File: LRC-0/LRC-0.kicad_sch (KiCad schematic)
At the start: 69 parts, among them J1 USB_C_Receptacle_USB2.0_14P, J2 Battery, J3 Conn_01x10, J4 SMA, J5 u.FL, SW1 EN, SW2 BOOT, U1 AP7361C-33E, U2 TVS1400DRV, U3 BQ24075RGT, U4 ESP32-C6-MINI-1, U5 SX1262IMLTRT, U6 4259-63, U8 4259-63, Y1 TX32-33015S-32.000-X-R

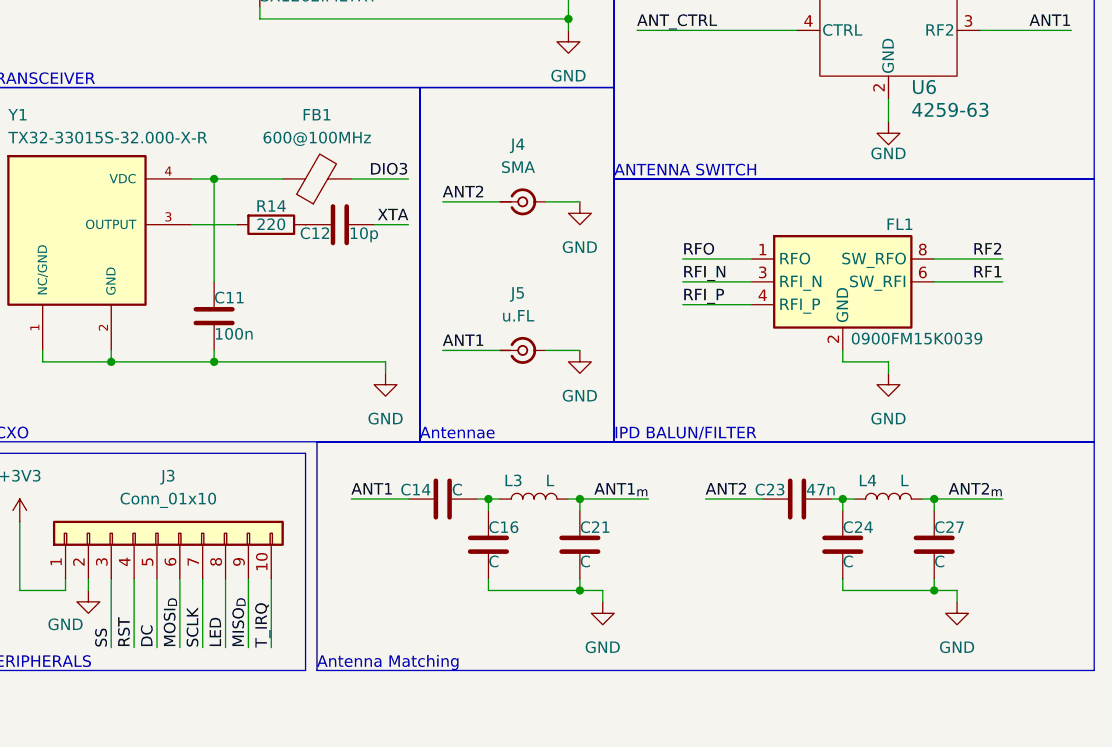
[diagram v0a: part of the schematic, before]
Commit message: rf route for filter and transceiver
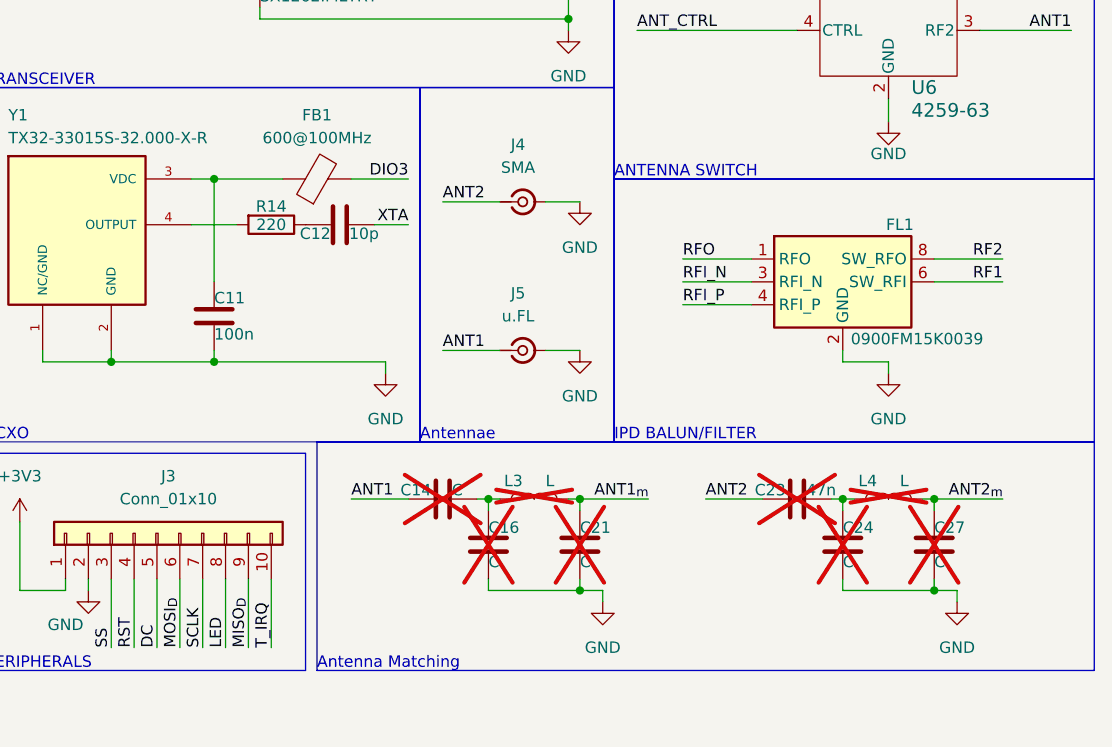
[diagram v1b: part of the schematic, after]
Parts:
- C14, C16, C21, C23, C24, C27, L3, L4: now not fitted
- L2: footprint Inductor_SMD:L_0402_1005Metric -> Inductor_SMD:L_0603_1608Metric
- U4: footprint RF_Module:ESP32-C6-MINI-1 -> ESP32_C6_MINI_1U_H4:XCVR_ESP32-C6-MINI-1U-H4
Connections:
- net at C11.1, FB1.1: now also Y1.3 (VDC); no longer Y1.4 (VDC)
- net at R14.2: now also Y1.4 (OUTPUT); no longer Y1.3 (OUTPUT)

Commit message: first pass done
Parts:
- C14, C16, C21, C23, C24, C27, L3, L4: now left out of the parts list
- L2: footprint Inductor_SMD:L_0603_1608Metric -> Inductor_SMD:L_1008_2520Metric
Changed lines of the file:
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@@
 		(unit 1)
 		(body_style 1)
-		(exclude_from_sim no)
-		(in_bom yes)
-		(on_board yes)
-		(in_pos_files yes)
+		(exclude_from_sim yes)
+		(in_bom no)
+		(on_board no)
+		(in_pos_files no)
 		(dnp yes)
 		(property "Reference" "C14"
@@
 		(unit 1)
 		(body_style 1)
-		(exclude_from_sim no)
-		(in_bom yes)
-		(on_board yes)
-		(in_pos_files yes)
+		(exclude_from_sim yes)
+		(in_bom no)
+		(on_board no)
+		(in_pos_files no)
 		(dnp yes)
 		(property "Reference" "C21"
@@
 		(unit 1)
 		(body_style 1)
-		(exclude_from_sim no)
-		(in_bom yes)
-		(on_board yes)
-		(in_pos_files yes)
+		(exclude_from_sim yes)
+		(in_bom no)
+		(on_board no)
+		(in_pos_files no)
 		(dnp yes)
 		(property "Reference" "L3"
@@
 		(unit 1)
 		(body_style 1)
-		(exclude_from_sim no)
-		(in_bom yes)
-		(on_board yes)
-		(in_pos_files yes)
+		(exclude_from_sim yes)
+		(in_bom no)
+		(on_board no)
+		(in_pos_files no)
 		(dnp yes)
 		(property "Reference" "C23"
@@
 		(unit 1)
 		(body_style 1)
-		(exclude_from_sim no)
-		(in_bom yes)
-		(on_board yes)
-		(in_pos_files yes)
+		(exclude_from_sim yes)
+		(in_bom no)
+		(on_board no)
+		(in_pos_files no)
 		(dnp yes)
 		(property "Reference" "C16"
@@
 		(unit 1)
 		(body_style 1)
-		(exclude_from_sim no)
-		(in_bom yes)
-		(on_board yes)
-		(in_pos_files yes)
+		(exclude_from_sim yes)
+		(in_bom no)
+		(on_board no)
+		(in_pos_files no)
 		(dnp yes)
 		(property "Reference" "C27"
@@
 			)
 		)
-		(property "Footprint" "Inductor_SMD:L_0603_1608Metric"
+		(property "Footprint" "Inductor_SMD:L_1008_2520Metric"
 			(at 195.58 40.64 0)
 			(hide yes)
@@
 		(unit 1)
 		(body_style 1)
-		(exclude_from_sim no)
-		(in_bom yes)
-		(on_board yes)
-		(in_pos_files yes)
+		(exclude_from_sim yes)
+		(in_bom no)
+		(on_board no)
+		(in_pos_files no)
 		(dnp yes)
 		(property "Reference" "C24"
@@
 		(unit 1)
 		(body_style 1)
-		(exclude_from_sim no)
-		(in_bom yes)
-		(on_board yes)
-		(in_pos_files yes)
+		(exclude_from_sim yes)
+		(in_bom no)
+		(on_board no)
+		(in_pos_files no)
 		(dnp yes)
 		(property "Reference" "L4"

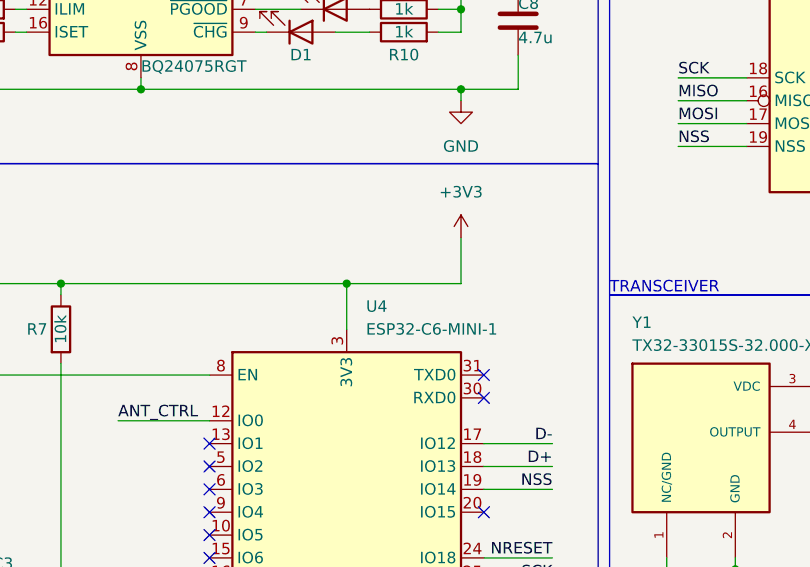
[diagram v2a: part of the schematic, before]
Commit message: shielding and pd redesign
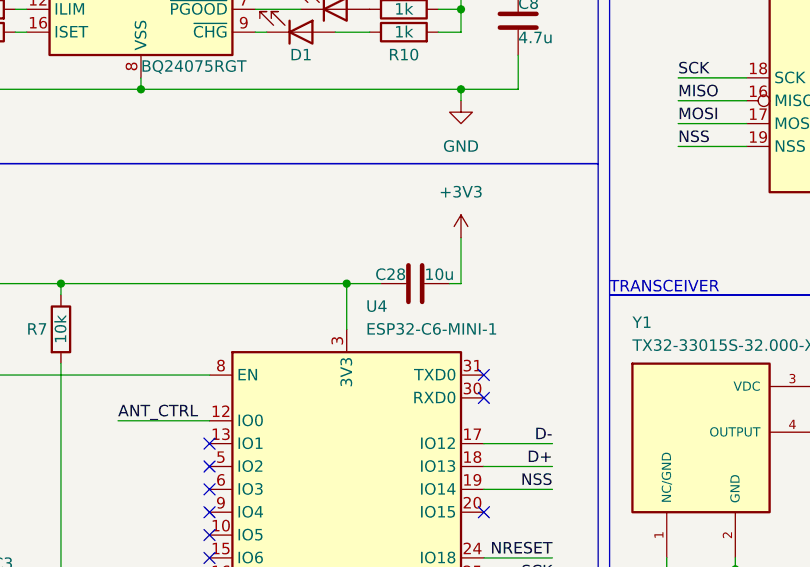
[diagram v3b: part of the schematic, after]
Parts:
- added C28: 10u, Capacitor_SMD:C_0402_1005Metric, symbol Device:C
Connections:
- net +3V3: now also C28.2; no longer R3.1, R7.1, U4.3 (3V3)
- new net: C28.1, R3.1, R7.1, U4.3 (3V3)
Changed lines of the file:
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@@
 	(wire
 		(pts
-			(xy 129.54 88.9) (xy 116.84 88.9)
+			(xy 129.54 88.9) (xy 128.27 88.9)
+		)
+		(stroke
+			(width 0)
+			(type default)
+		)
+	)
+	(wire
+		(pts
+			(xy 120.65 88.9) (xy 116.84 88.9)
 		)
 		(stroke
@@
 					(unit 1)
 				)
+			)
+		)
+	)
+	(symbol
+		(lib_id "Device:C")
+		(at 124.46 88.9 90)
+		(mirror x)
+		(unit 1)
+		(body_style 1)
+		(exclude_from_sim no)
+		(in_bom yes)
+		(on_board yes)
+		(in_pos_files yes)
+		(dnp no)
+		(property "Reference" "C28"
+			(at 123.444 88.646 90)
+			(show_name no)
+			(do_not_autoplace no)
+			(effects
+				(font
+					(size 1.27 1.27)
+				)
+				(justify left bottom)
+			)
+		)
+		(property "Value" "10u"
+			(at 125.476 88.646 90)
+			(show_name no)
+			(do_not_autoplace no)
+			(effects
+				(font
+					(size 1.27 1.27)
+				)
+				(justify right bottom)
+			)
+		)
+		(property "Footprint" "Capacitor_SMD:C_0402_1005Metric"
+			(at 128.27 89.8652 0)
+			(hide yes)
+			(show_name no)
+			(do_not_autoplace no)
+			(effects
+				(font
+					(size 1.27 1.27)
+				)
+			)
+		)
+		(property "Datasheet" ""
+			(at 124.46 88.9 0)
+			(hide yes)
+			(show_name no)
+			(do_not_autoplace no)
+			(effects
+				(font
+					(size 1.27 1.27)
+				)
+			)
+		)
+		(property "Description" "Unpolarized capacitor"
+			(at 124.46 88.9 0)
+			(hide yes)
+			(show_name no)
+			(do_not_autoplace no)
+			(effects
+				(font
+					(size 1.27 1.27)
+				)
+			)
+		)
+		(pin "2"
+		)
+		(pin "1"
+		)
+		(instances
+			(project "LRC-0"
+				(path "/a4fcac9a-bf35-4c24-be09-41c3c4d3bdce"
+					(reference "C28")
+					(unit 1)
+				)

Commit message: stitching
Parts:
- removed C28: 10u, Capacitor_SMD:C_0402_1005Metric, symbol Device:C
- removed H1, H2, H3, H4: MountingHole, MountingHole:MountingHole_2.2mm_M2, symbol Mechanical:MountingHole
- added H1, H2, H3, H4: MountingHole_Pad_MP, symbol Mechanical:MountingHole_Pad_MP
- added SW3: SW_SPDT, Connector_PinHeader_1.00mm:PinHeader_1x02_P1.00mm_Vertical, symbol Switch:SW_SPDT
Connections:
- net +3V3: now also R3.1, R7.1, U4.3 (3V3)
- net VCC: now also U3.5 (EN2), SW3.1 (A); no longer C6.1, C7.1, R10.2, R9.1, U3.10 (OUT), U3.11 (OUT)
- net +5V renamed VBUS
- net VBUS: no longer U3.5 (EN2)
- net GND renamed Earth_Protective
- net Earth_Protective: now also H1.MP, H2.MP, H3.MP, H4.MP
- new net VOUT: C6.1, C7.1, R10.2, R9.1, SW3.2 (B), U3.10 (OUT), U3.11 (OUT)
- no-connect marks 20 -> 21
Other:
- moved on the sheet: C1, C2, U1

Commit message: bom and jlcpcb quote
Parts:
- H1, H2, H3, H4: footprint (none) -> MountingHole:MountingHole_2.2mm_M2_Pad_TopOnly
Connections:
- net Earth_Protective: no longer C11.2, Y1.1 (NC/GND), Y1.2 (GND)
- new net: Y1.1 (NC/GND), Y1.2 (GND)
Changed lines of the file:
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@@
 	)
 	(junction
-		(at 171.45 120.65)
-		(diameter 0)
-		(color 0 0 0 0)
-	)
-	(junction
 		(at 251.46 135.89)
 		(diameter 0)
@@
 	)
 	(junction
-		(at 160.02 120.65)
-		(diameter 0)
-		(color 0 0 0 0)
-	)
-	(junction
 		(at 115.57 30.48)
 		(diameter 0)
@@
 	(wire
 		(pts
-			(xy 160.02 120.65) (xy 171.45 120.65)
-		)
-		(stroke
-			(width 0)
-			(type default)
-		)
-	)
-	(wire
-		(pts
 			(xy 33.02 124.46) (xy 33.02 130.81)
 		)
@@
 	(wire
 		(pts
-			(xy 171.45 120.65) (xy 190.5 120.65)
-		)
-		(stroke
-			(width 0)
-			(type default)
-		)
-	)
-	(wire
-		(pts
 			(xy 218.44 40.64) (xy 227.33 40.64)
 		)
@@
 			)
 		)
-		(property "Footprint" ""
+		(property "Footprint" "MountingHole:MountingHole_2.2mm_M2_Pad_TopOnly"
 			(at 35.56 111.76 0)
 			(hide yes)
@@
 			)
 		)
-		(property "Footprint" ""
+		(property "Footprint" "MountingHole:MountingHole_2.2mm_M2_Pad_TopOnly"
 			(at 35.56 118.11 0)
 			(hide yes)
@@
 			)
 		)
-		(property "Footprint" ""
+		(property "Footprint" "MountingHole:MountingHole_2.2mm_M2_Pad_TopOnly"
 			(at 35.56 124.46 0)
 			(hide yes)
@@
 			)
 		)
-		(property "Footprint" ""
+		(property "Footprint" "MountingHole:MountingHole_2.2mm_M2_Pad_TopOnly"
 			(at 35.56 130.81 0)
 			(hide yes)
